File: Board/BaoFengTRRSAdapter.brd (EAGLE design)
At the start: 35.5 x 10.7 mm, 9 parts

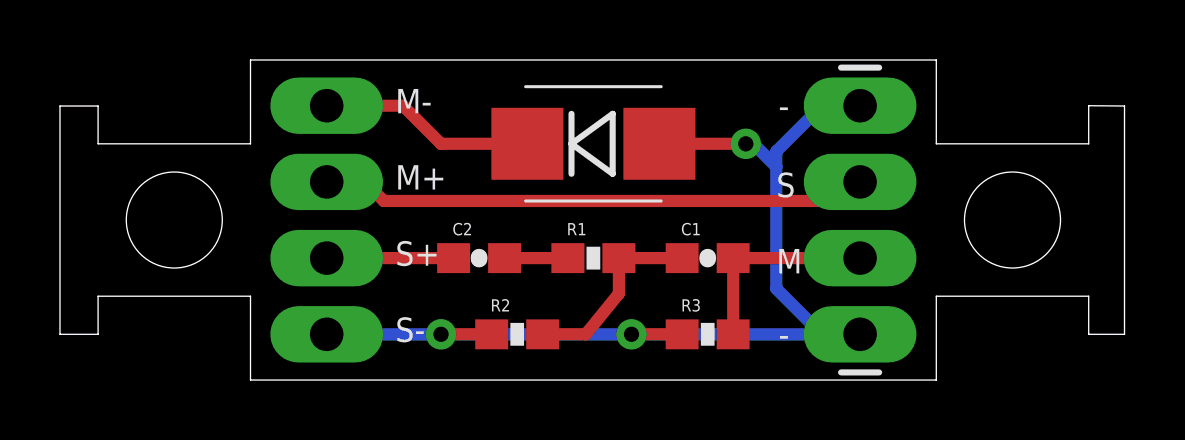
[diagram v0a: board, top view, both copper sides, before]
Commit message: Removing unnecessary diode, making board a bit smaller
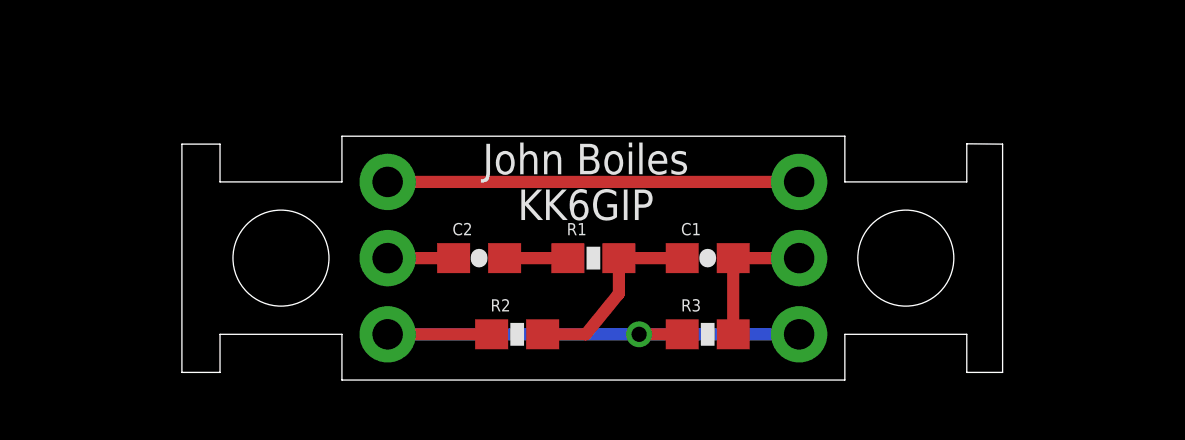
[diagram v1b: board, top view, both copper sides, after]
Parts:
- removed D1: (no value), SparkFun-DiscreteSemi:SMB-DIODE
- removed JP2: M02PTH3, SparkFun-Connectors:1X02_LONGPADS
- JP1: value M02PTH3 -> (none); device SparkFun-Connectors:1X02_LONGPADS -> SparkFun-Connectors:1X03_NO_SILK
- JP3: device SparkFun-Connectors:1X04_LONGPADS -> SparkFun-Connectors:1X03_NO_SILK
- moved JP1 3.25 mm to (10.9, 2.54), turned to 90 degrees
- moved JP3 2.03 mm to (24.6, 2.54)
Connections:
- removed net BAOFENGMIC-: D1.C, JP2.2
- removed net BAOFENGSPK+: C2.2, JP1.1
- new net N$1: C2.2, JP1.2
- net BAOFENGMIC+: now also JP1.3; no longer JP2.1
- net GND: now also JP1.1; no longer D1.A, JP1.2, JP3.4
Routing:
- net GND: track 35.5 -> 18.6 mm, vias 3 -> 1
- net BAOFENGMIC-: track 7.22 -> 0.00 mm
- net BAOFENGMIC+: track 18.3 -> 13.7 mm
- net BAOFENGSPK+: track 4.23 -> 0.00 mm
- net N$1: track 0.00 -> 2.20 mm
- net N$4: track 6.77 -> 4.74 mm
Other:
- board size 35.5 x 10.7 mm -> 27.4 x 8.1 mm
- board text added: "TRRS"
- board text added: "UV5R"
- board text added: "r2"
- board text removed: "Baofeng UV5R TRRS Adapter"
- board text removed: "M-"
- board text removed: "r1"
